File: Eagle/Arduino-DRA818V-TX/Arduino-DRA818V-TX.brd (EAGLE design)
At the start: 68.6 x 53.3 mm, 23 parts, among them M1 ARDUINO_R3_ICSP, X1 SMA, X2 SMA

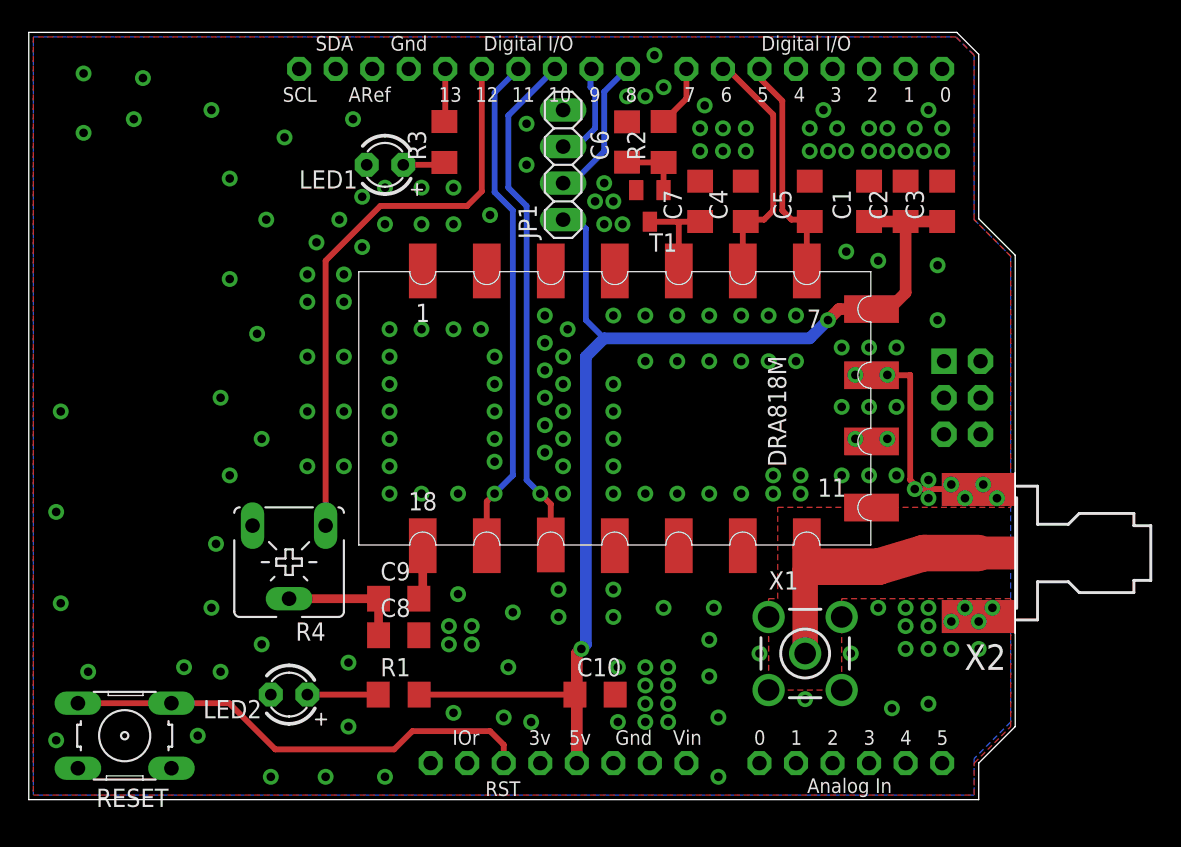
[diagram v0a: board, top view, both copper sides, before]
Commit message: Using 0805 SMDs
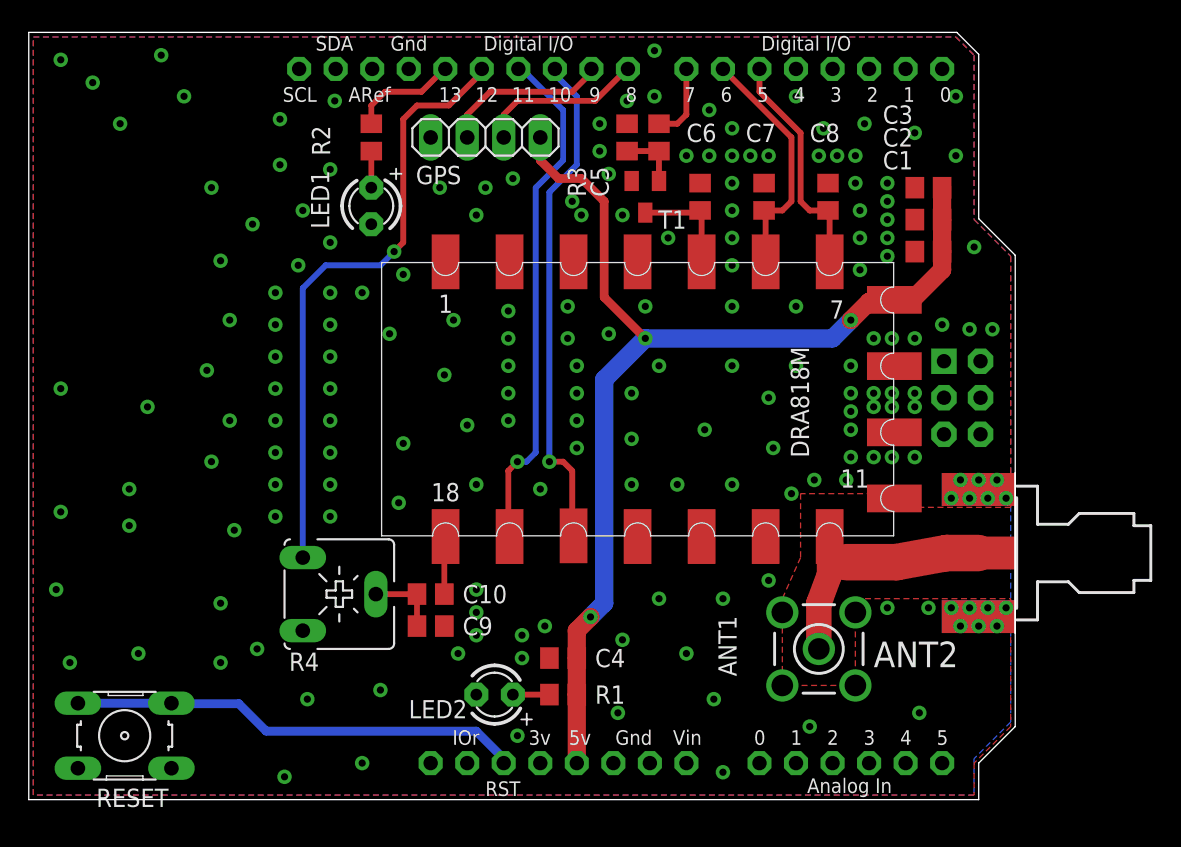
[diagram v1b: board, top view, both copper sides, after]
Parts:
- removed JP1: (no value), pinhead:1X04
- removed X1: SMA, con-coax:LTI-SASF54GT
- added ANT1: 50 Z, con-coax:LTI-SASF54GT
- added GPS: + TX RX GND, pinhead:1X04
- ANT2: value SMA -> 50 Z
- C1, C10, C2, C5, C6, C7, C8: device resistor:C1206 -> resistor:C0805
- C3, C9: value 1u -> 100n; device resistor:C1206 -> resistor:C0805
- C4: value 100n -> 1u; device resistor:C1206 -> resistor:C0805
- R1: device resistor:R1206 -> resistor:R0805
- R2: value 1k -> 560; device resistor:R1206 -> resistor:R0805
- R3: value 560 -> 5k6; device resistor:R1206 -> resistor:R0805
- moved C8 42.7 mm to (70.2, 73.7), turned to 90 degrees
- moved C4 34.2 mm to (51.8, 41.6), turned to 180 degrees
- moved R2 20.3 mm to (38.4, 77.8)
- moved R3 14.9 mm to (58.4, 77.8)
- moved LED2 14.3 mm to (47.0, 39.1)
- moved C5 13.5 mm to (56.2, 77.8)
- moved C10 13.4 mm to (42.5, 46.0)
- moved R1 11.4 mm to (51.8, 39.1)
- moved C6 6.35 mm to (61.3, 73.7)
- moved C1 5.41 mm to (77.2, 69.8), turned to 180 degrees
- moved C7 4.46 mm to (65.7, 73.7)
- moved R4 4.14 mm to (36.2, 46.0), turned to 270 degrees
- moved LED1 3.01 mm to (38.4, 73.0), turned to 270 degrees
- moved C9 2.93 mm to (42.5, 43.8)
- moved C2 2.03 mm to (77.2, 72.1), turned to 180 degrees
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- renumbered X2 to ANT2
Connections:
- net +5V: now also C4.1, GPS.1; no longer C10.1, JP1.1
- net AF_NORM: now also C10.2; no longer C9.2
- net GND: now also ANT1.2, ANT1.3, ANT1.4, ANT1.5, C9.2, GPS.4; no longer C10.2, JP1.4, X1.2, X1.3, X1.4, X1.5
- net LED_BUILTIN: now also R2.2; no longer R3.2
- net N$5: now also ANT1.1; no longer X1.1
- net N$7: now also C5.1, R3.1; no longer C6.1, R2.1
- net N$8: now also R2.1; no longer R3.1
- net N$9: now also C10.1; no longer C8.1
- net PD: now also C7.1; no longer C4.1
- net POW: now also C8.1; no longer C5.1
- net PTT: now also R3.2; no longer R2.2
- net PTT_SW: now also C6.1; no longer C7.1
- net RXD_GPS: now also GPS.2; no longer JP1.2
- net TXD_GPS: now also GPS.3; no longer JP1.3
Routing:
- net GND: track 18.6 -> 0.00 mm, vias 213 -> 188
- net +5V: track 83.6 -> 77.9 mm, vias 2 -> 3
- net TXD_GPS: track 7.03 -> 11.7 mm
- net LED_BUILTIN: track 3.68 -> 7.47 mm
- net N$9: track 8.76 -> 5.08 mm
- net AF_OUT: track 39.8 -> 42.7 mm, vias 0 -> 1
- net N$41: track 4.93 -> 2.54 mm
- net RXD_GPS: track 10.2 -> 11.5 mm
- net RESET: track 33.1 -> 32.1 mm
- net PTT: track 4.32 -> 5.34 mm
- net TXD_DRJ: track 35.1 -> 36.0 mm
- net RXD_DRJ: track 35.7 -> 35.1 mm
- net PTT_SW: track 6.96 -> 7.49 mm
